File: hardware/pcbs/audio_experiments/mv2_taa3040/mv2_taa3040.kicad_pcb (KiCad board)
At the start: 4 copper layers, 118 x 48 mm, 120 parts, among them J1 MTA100-3, J2 MTA100-3, J3 MTA100-3, J4 Interconnect, J5 MTA100-3, Q1 2N7002, Q2 SI2309CDS-T1-GE3, Q3 2N7002, Q4 SI2309CDS-T1-GE3, Q5 2N7002, Q6 SI2309CDS-T1-GE3, Q7 2N7002, Q8 SI2309CDS-T1-GE3, U1 TCA9534, U2 TAA3040, U3 LP5907MFX-3.3

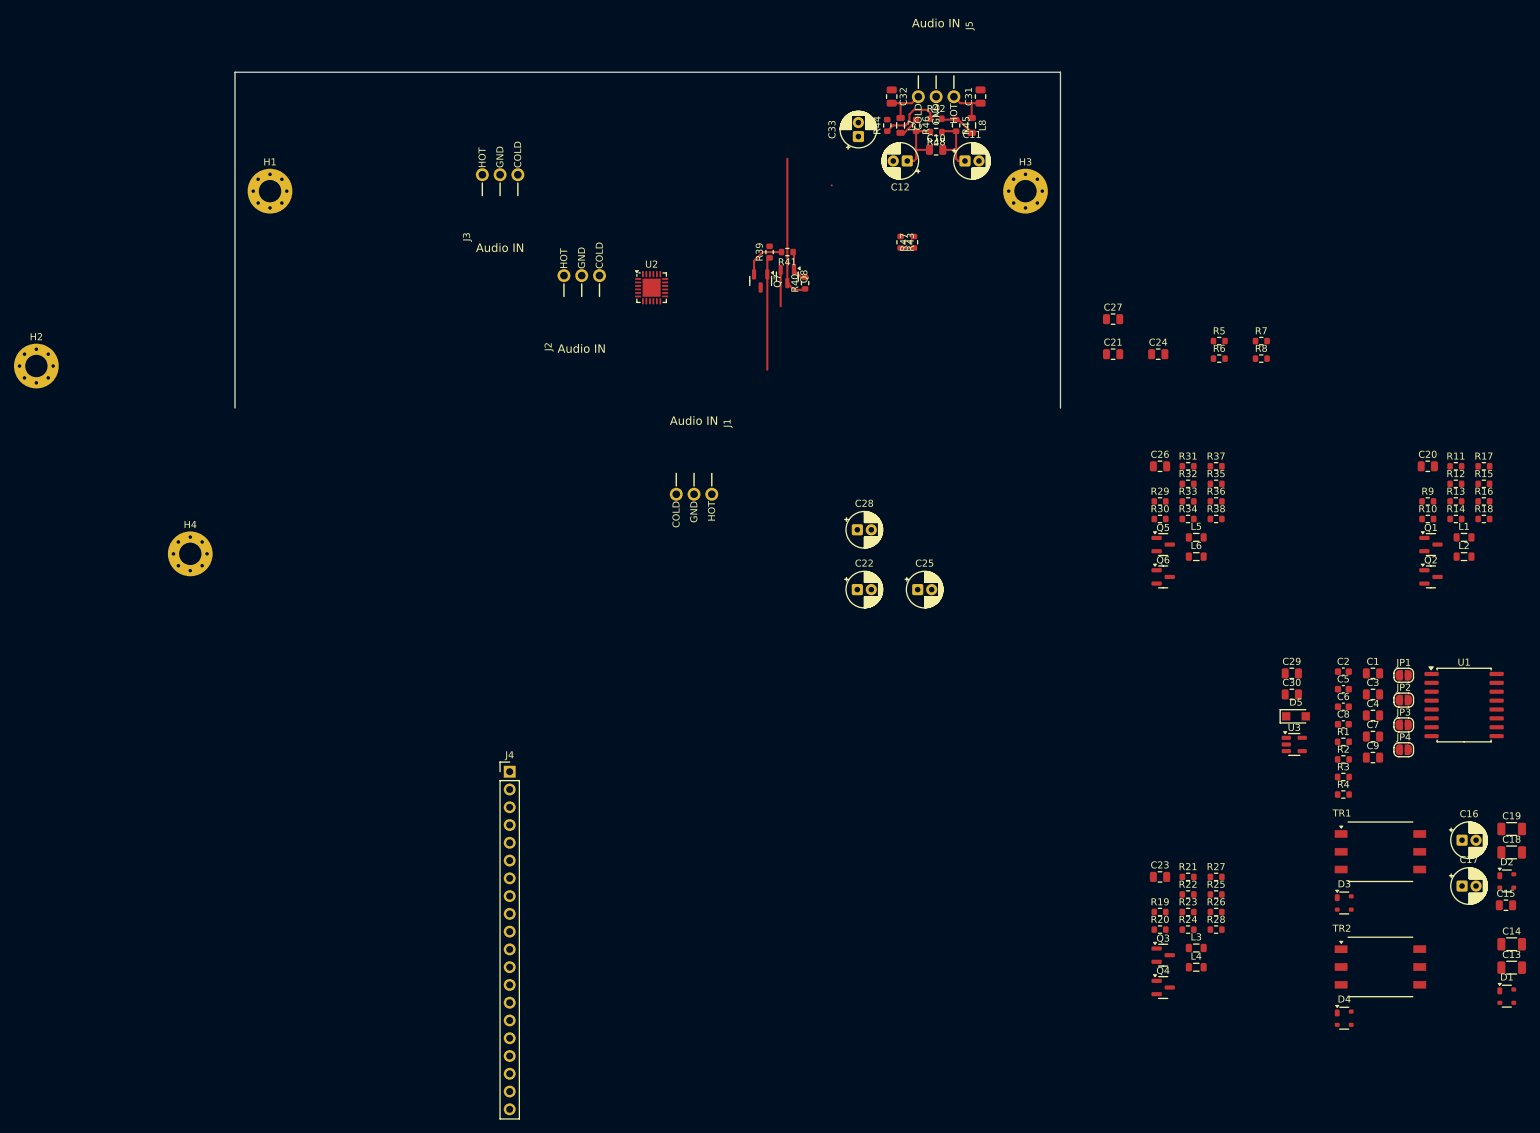
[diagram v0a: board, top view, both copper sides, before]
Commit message: replicate frontend layout
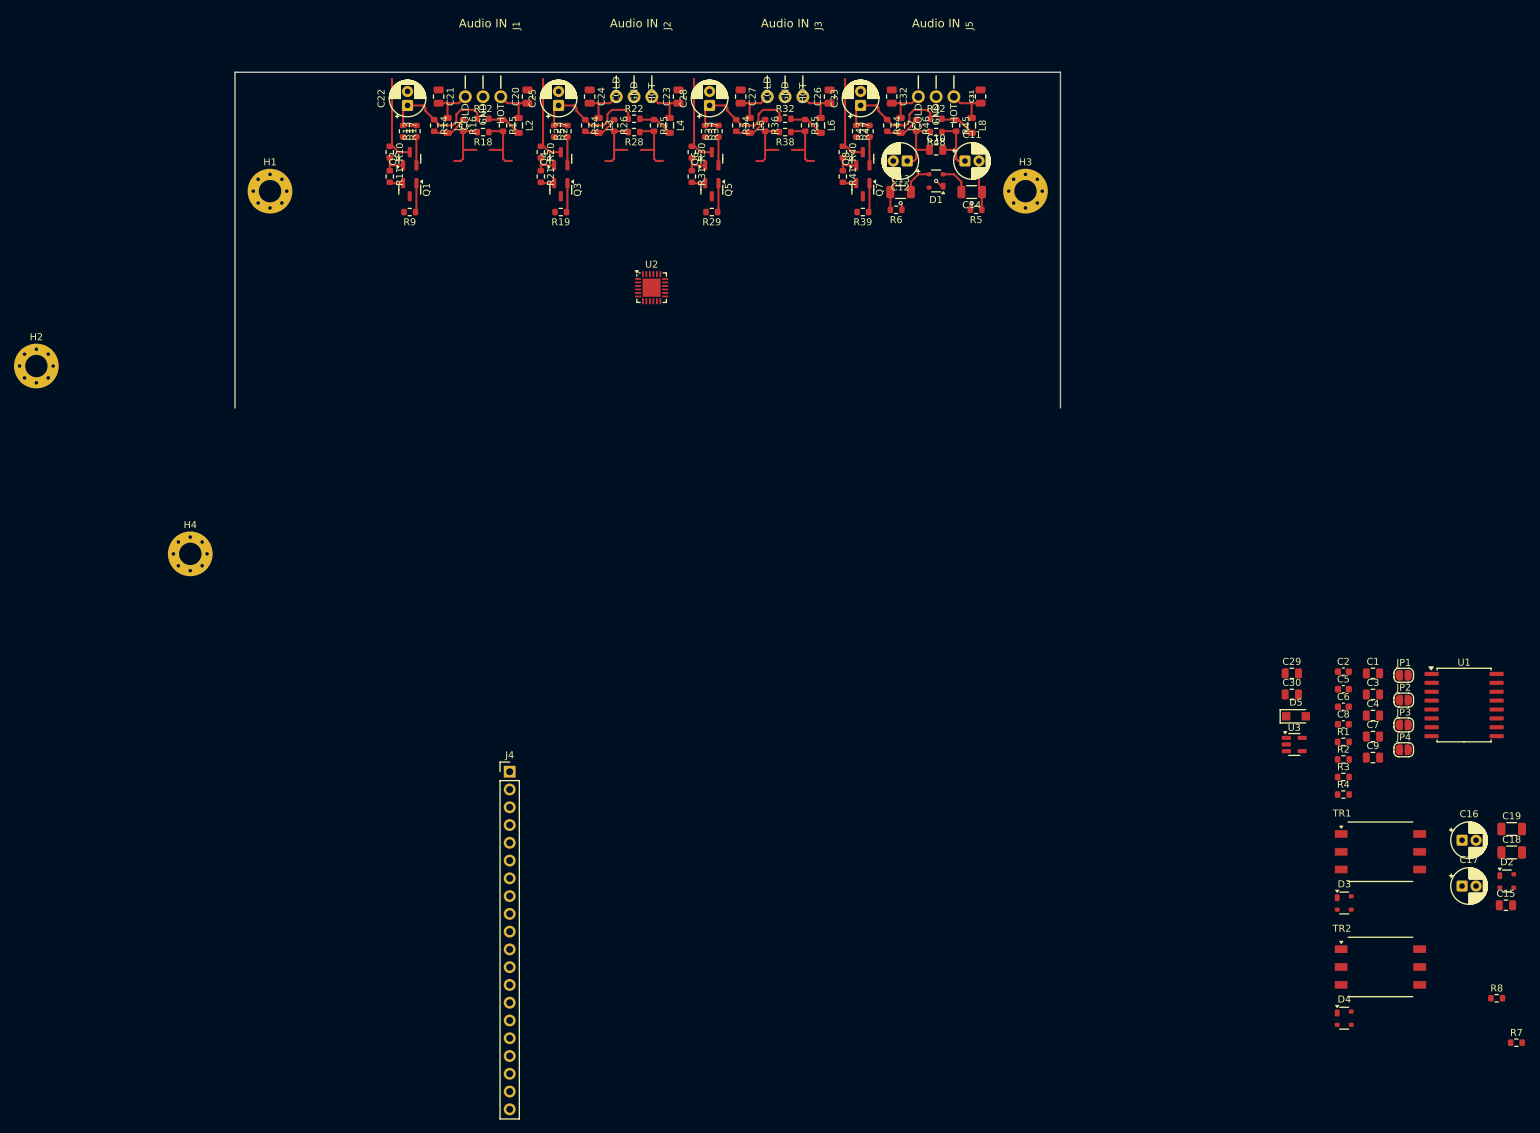
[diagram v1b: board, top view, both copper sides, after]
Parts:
- moved R17 161.8 mm to (9.53, -4.57), turned to -90 degrees
- moved R11 157.9 mm to (7.62, 1.91), turned to -90 degrees
- moved Q2 157.7 mm to (10.5, -0.63), turned to 90 degrees
- moved R13 157.7 mm to (11.4, -4.57), turned to 90 degrees
- moved R10 157.4 mm to (7.62, -1.58), turned to -90 degrees
- moved L1 156.8 mm to (15.9, -5.39), turned to -90 degrees
- moved R14 156.5 mm to (14.0, -5.39), turned to -90 degrees
- moved R16 155.5 mm to (18.1, -5.39), turned to -90 degrees
- moved Q1 154.5 mm to (10.5, 3.80), turned to -90 degrees
- moved R18 153.4 mm to (21.0, -4.44), turned to 180 degrees
- moved R9 151.3 mm to (10.5, 6.99), turned to 180 degrees
- moved R15 149.3 mm to (23.8, -5.39), turned to -90 degrees
- moved L2 148.5 mm to (26.0, -5.39), turned to -90 degrees
- moved R12 148.5 mm to (21.0, -6.35)
- moved Q4 146.5 mm to (32.1, -0.63), turned to 90 degrees
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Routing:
- net +48V: track 20.8 -> 49.9 mm
- net Net-(C28-Pad1): track 0.00 -> 19.0 mm
- net Net-(C25-Pad1): track 0.00 -> 19.0 mm
- net Net-(C22-Pad1): track 0.00 -> 19.0 mm
- net /Balanced Input 1/PHANTOM: track 16.1 -> 4.18 mm
- net /Balanced Input 4/Input frontend/HOT: track 0.00 -> 9.33 mm
- net /Balanced Input 2/Input frontend/HOT: track 0.00 -> 9.33 mm
- net /Balanced Input 3/Input frontend/HOT: track 0.00 -> 9.33 mm
- net /Balanced Input 4/Input frontend/COLD: track 0.00 -> 9.33 mm
- net /Balanced Input 3/Input frontend/COLD: track 0.00 -> 9.33 mm
- net /Balanced Input 2/Input frontend/COLD: track 0.00 -> 9.33 mm
- net Net-(C33-Pad1): track 10.9 -> 19.0 mm
- net Net-(C12-Pad2): track 0.00 -> 7.17 mm
- net Net-(C11-Pad2): track 0.00 -> 7.17 mm
- net Net-(J3-Pin_1): track 0.00 -> 6.31 mm
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
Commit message: test pcb almost done
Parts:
- moved D3 163.8 mm to (13.3, 6.99)
- moved TR1 160.0 mm to (20.0, 4.13), turned to -90 degrees
- moved D4 158.5 mm to (35.2, 6.99)
- moved R8 156.4 mm to (57.5, 6.67), turned to 180 degrees
- moved R7 155.3 mm to (68.9, 6.67), turned to 180 degrees
- moved TR2 154.2 mm to (41.9, 4.13), turned to -90 degrees
- moved U1 150.1 mm to (21.9, 21.6), turned to 180 degrees
- moved C15 149.9 mm to (63.2, -1.91)
- moved C17 145.3 mm to (59.1, -0.32), turned to 180 degrees
- moved C18 144.9 mm to (58.1, 4.13)
- moved D2 144.4 mm to (63.2, 2.54), turned to 180 degrees
- moved C19 135.1 mm to (68.3, 4.13), turned to 180 degrees
- moved C16 134.9 mm to (67.3, -0.32)
- moved JP4 131.1 mm to (38.1, 20.0), turned to 180 degrees
- moved JP3 130.6 mm to (38.1, 17.5), turned to 180 degrees
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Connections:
- D3 pad 2: /Balanced Input 4/HOT -> /Balanced Input 4/COLD
- D3 pad 3: /Balanced Input 4/COLD -> /Balanced Input 4/HOT
- D4 pad 2: /Balanced Input 3/HOT -> /Balanced Input 3/COLD
- D4 pad 3: /Balanced Input 3/COLD -> /Balanced Input 3/HOT
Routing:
- net /Balanced Input 1/PHANTOM: track 4.18 -> 71.4 mm, vias 0 -> 2
- net /Balanced Input 2/PHANTOM: track 4.18 -> 61.0 mm, vias 0 -> 2
- net /Conn and power/SCL: track 0.00 -> 46.8 mm, vias 0 -> 2
- net /Conn and power/SDA: track 0.00 -> 46.6 mm, vias 0 -> 2
- net /Balanced Input 4/COLD: track 0.00 -> 45.4 mm
- net /Balanced Input 4/HOT: track 0.00 -> 43.1 mm
- net /Balanced Input 1/HOT: track 4.52 -> 44.0 mm
- net /Balanced Input 1/COLD: track 4.52 -> 37.0 mm
- net +3.3V: track 0.00 -> 31.3 mm, vias 0 -> 2
- net +3.3VA: track 0.00 -> 30.4 mm, vias 0 -> 2
- net /Balanced Input 4/PHANTOM: track 4.18 -> 31.4 mm, vias 0 -> 2
- net /Balanced Input 2/HOT: track 0.00 -> 23.6 mm
- net /Balanced Input 3/COLD: track 0.00 -> 23.2 mm
- net /Balanced Input 3/HOT: track 0.00 -> 21.1 mm
- net /Balanced Input 3/PHANTOM: track 4.18 -> 22.6 mm, vias 0 -> 2
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- added copper zone on B.Cu, net GND
- added copper zone on F.Cu, net GND
- added copper zone on In1.Cu, net GND
- added copper zone on In2.Cu, net GND

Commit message: finalise board
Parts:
- added C1: 1μF, Capacitor_SMD:C_0805_2012Metric, F.Cu at (17.5, 28.3)
- moved H2 108.6 mm to (65.6, 34.7), turned to -90 degrees
- moved H4 67.2 mm to (0.00, -8.00)
- moved H1 28.8 mm to (10.6, 24.7), turned to -90 degrees
- moved J4 24.1 mm to (57.1, 31.0), turned to -90 degrees
- moved H3 11.9 mm to (98.7, -7.94)
- renumbered C9 to C10, C10 to C11, C11 to C12, C12 to C13, C13 to C14, C14 to C15, C15 to C16, C16 to C17, C17 to C18, C18 to C19, C1 to C2, C19 to C20, C20 to C21, C21 to C22, C22 to C23, C23 to C24, C24 to C25, C25 to C26, C26 to C27, C27 to C28, C28 to C29, C2 to C3, C29 to C30, C30 to C31, C31 to C32, C32 to C33, C33 to C34, C3 to C4, C4 to C5, C5 to C6, C6 to C7, C7 to C8, C8 to C9
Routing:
- net +48V: track 49.9 -> 205.1 mm
- net +3.3VA: track 30.4 -> 116.7 mm, vias 2 -> 7
- net +5VA: track 5.92 -> 47.2 mm, vias 0 -> 2
- net +3.3V: track 31.3 -> 69.5 mm, vias 2 -> 4
- net /Conn and power/I2S_BCLK: track 7.82 -> 32.6 mm, vias 1 -> 2
- net /Conn and power/I2S_MCLK: track 7.64 -> 30.8 mm, vias 1 -> 2
- net /Conn and power/I2S_RX: track 8.01 -> 29.3 mm, vias 1 -> 2
- net /Balanced Input 2/PHANTOM: track 61.0 -> 51.3 mm
- net /Conn and power/SCL: track 46.8 -> 51.5 mm, vias 2 -> 3
- net GND: track 15.2 -> 19.5 mm, vias 17 -> 60
- net /Conn and power/SDA: track 46.6 -> 50.4 mm
- net /Balanced Input 1/PHANTOM: track 71.4 -> 68.1 mm
- net /Balanced Input 1/HOT: track 44.0 -> 41.5 mm
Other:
- board size 118 x 48 mm -> 108.5 x 53 mm
- board text added: "+12V"
- board text added: "+3V3"
- board text added: "+48V"
- board text added: "+5V"
- board text added: "+5VA"
- board text added: "-12V"
- board text added: "ADC board revA"
- board text added: "BCLK"
- board text added: "CS"
- board text added: "Conn_01x20"
- board text added: "GND"
- board text added: "I2S RX"
- board text added: "I2S TX"
- board text added: "LRCLK"
- board text added: "MCLK"
- board text added: "MISO"
- board text added: "MOSI"
- board text added: "SCK"
- board text added: "SCL"
- board text added: "SDA"
